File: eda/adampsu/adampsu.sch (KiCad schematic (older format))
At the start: 45 parts, among them J1 Barrel_Jack_Switch, J2 Conn_2Rows-09Pins, J3 DB9_Female, Q1 BUK7880-55A_CUX, SW1 30V 300mA Latching Switch, U1 LM27761, U2 TPS54531DDAR

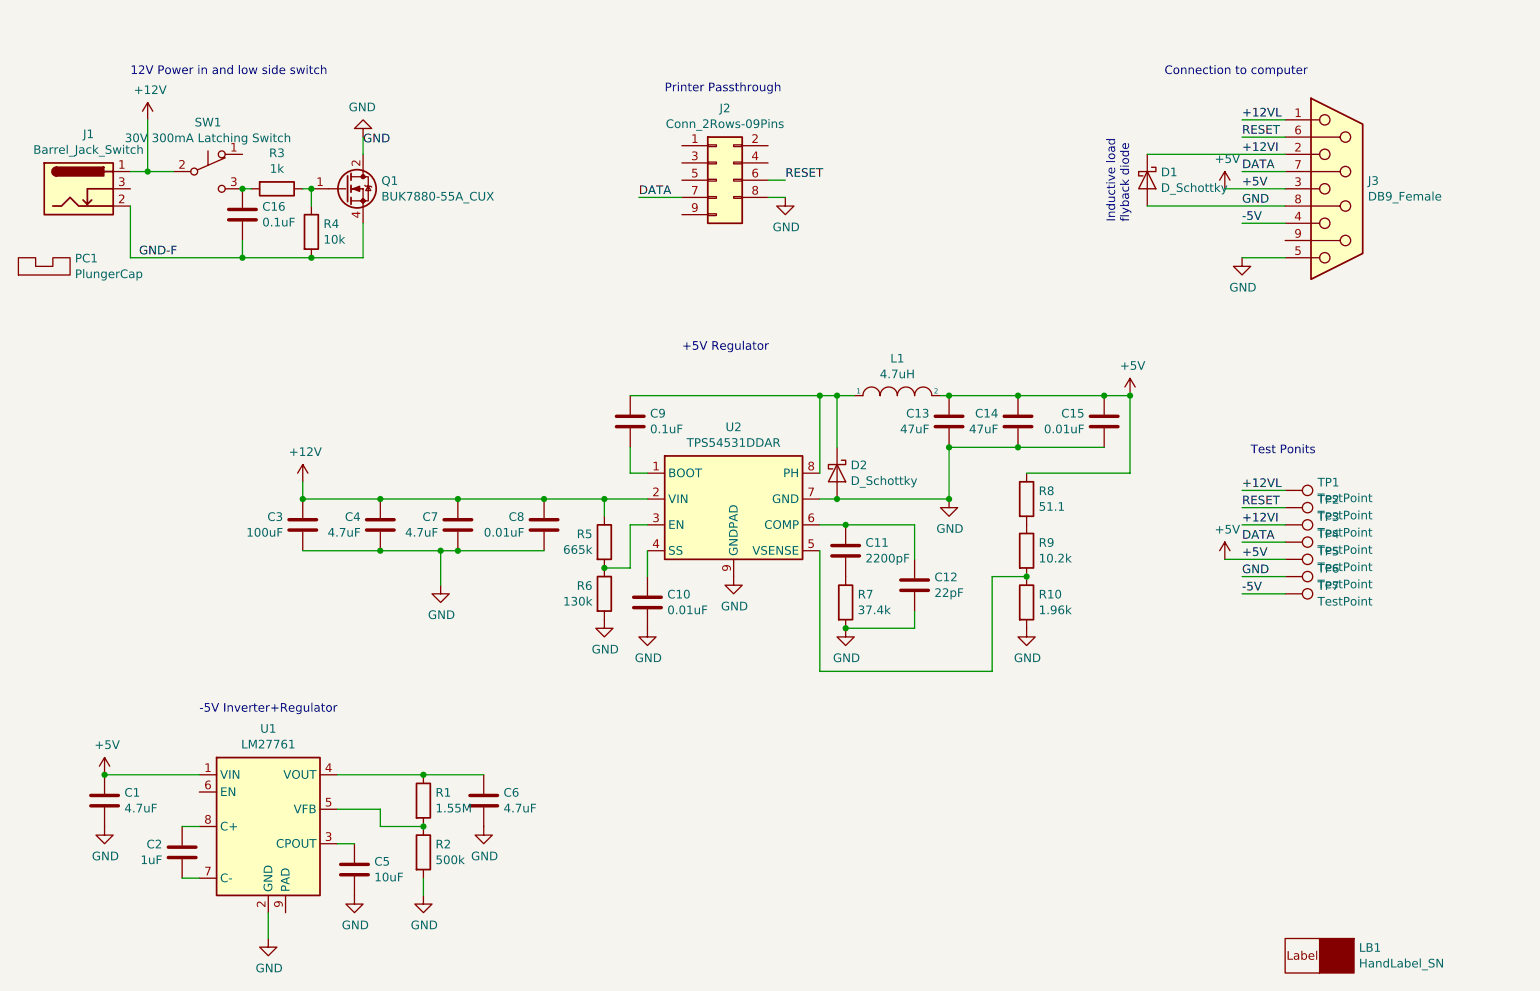
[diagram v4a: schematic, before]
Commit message: using non-inverting buck for negative, too expensive though
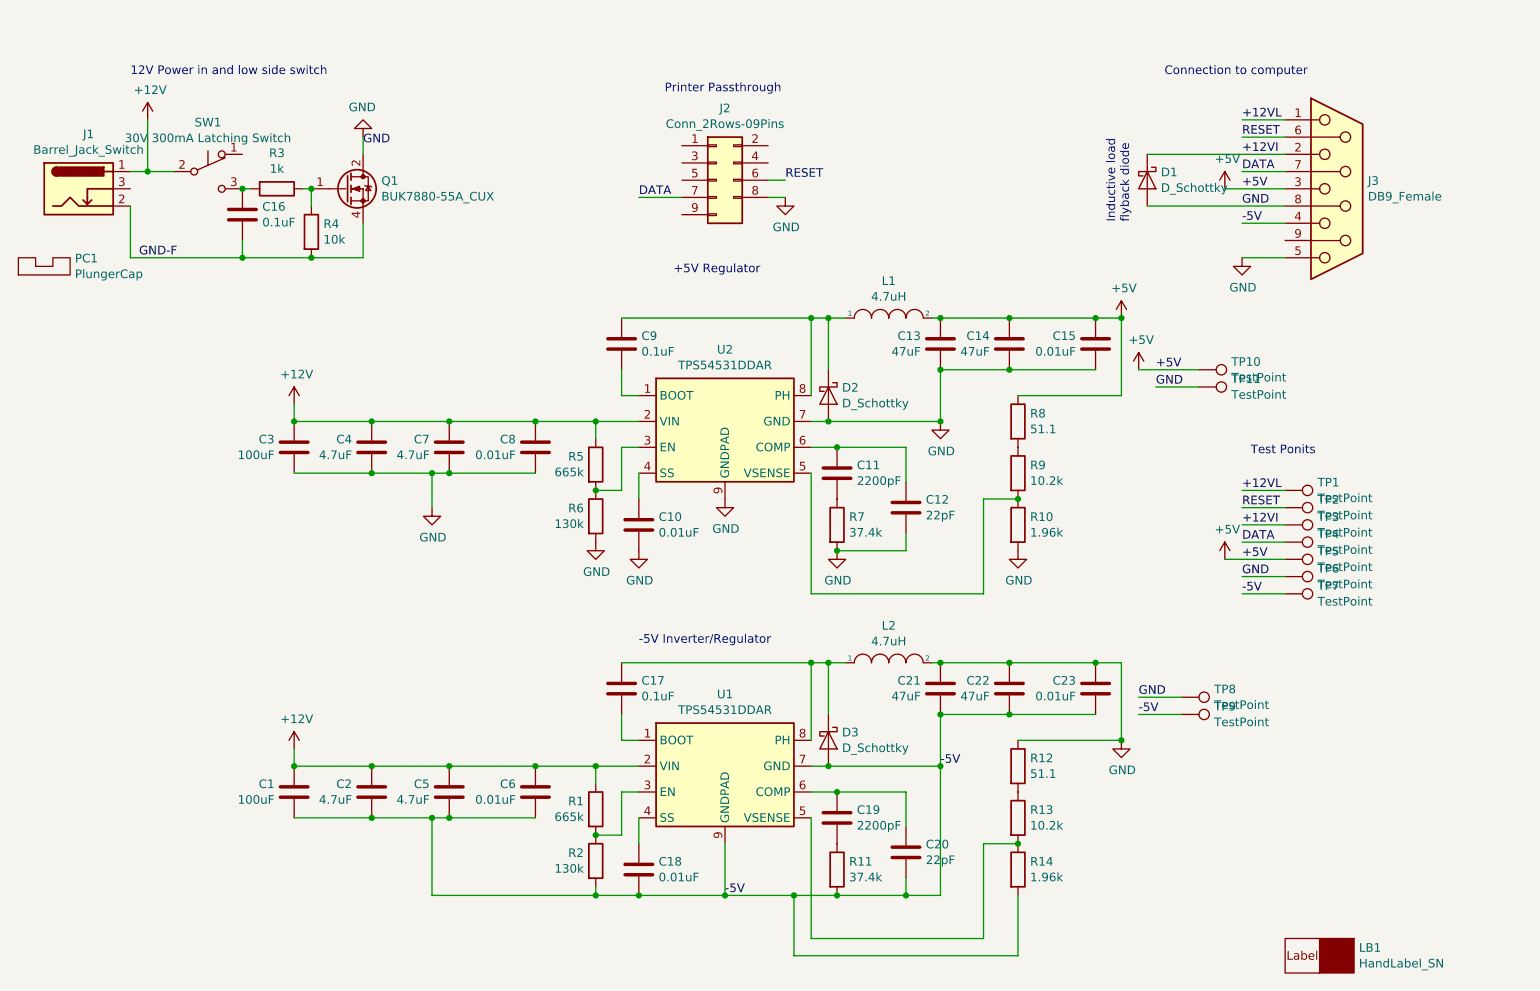
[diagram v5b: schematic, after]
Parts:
- removed R1: 1.55M, Resistor_SMD:R_0603_1608Metric_Pad1.05x0.95mm_HandSolder, symbol adampsu-rescue:R-Device
- removed R2: 500k, Resistor_SMD:R_0603_1608Metric_Pad1.05x0.95mm_HandSolder, symbol adampsu-rescue:R-Device
- removed U1: LM27761, Package_SON:WSON-8-1EP_2x2mm_P0.5mm_EP0.9x1.6mm, symbol adampsu-rescue:LM27761-Regulator_SwitchedCapacitor
- added C17: 0.1uF, adampsu:C_0508_1220Metric_Pad1.40x1.15mm_HandSolder, symbol Device:C
- added C18, C23: 0.01uF, Capacitor_SMD:C_0603_1608Metric_Pad1.05x0.95mm_HandSolder, symbol adampsu-rescue:C-Device
- added C19: 2200pF, Capacitor_SMD:C_0603_1608Metric_Pad1.05x0.95mm_HandSolder, symbol Device:C
- added C20: 22pF, Capacitor_SMD:C_0603_1608Metric_Pad1.05x0.95mm_HandSolder, symbol Device:C
- added C21, C22: 47uF, Capacitor_SMD:C_1210_3225Metric_Pad1.42x2.65mm_HandSolder, symbol adampsu-rescue:C-Device
- added D3: D_Schottky, Diode_SMD:D_SMC_Handsoldering, symbol Device:D_Schottky
- added L2: 4.7uH, adampsu:L_11.5x10.3_H4.8, symbol pspice:INDUCTOR
- added R1: 665k, Resistor_SMD:R_0603_1608Metric_Pad1.05x0.95mm_HandSolder, symbol Device:R
- added R11: 37.4k, Resistor_SMD:R_0603_1608Metric_Pad1.05x0.95mm_HandSolder, symbol Device:R
- added R12: 51.1, Resistor_SMD:R_0603_1608Metric_Pad1.05x0.95mm_HandSolder, symbol Device:R
- added R13: 10.2k, Resistor_SMD:R_0603_1608Metric_Pad1.05x0.95mm_HandSolder, symbol Device:R
- added R14: 1.96k, Resistor_SMD:R_0603_1608Metric_Pad1.05x0.95mm_HandSolder, symbol Device:R
- added R2: 130k, Resistor_SMD:R_0603_1608Metric_Pad1.05x0.95mm_HandSolder, symbol Device:R
- added TP10, TP11, TP8, TP9: TestPoint, TestPoint:TestPoint_THTPad_2.0x2.0mm_Drill1.0mm, symbol Connector:TestPoint
- added U1: TPS54531DDAR, Package_SO:TI_SO-PowerPAD-8_ThermalVias, symbol Custom:TPS54531DDAR
- C1: value 4.7uF -> 100uF; footprint Capacitor_SMD:C_1206_3216Metric_Pad1.42x1.75mm_HandSolder -> Capacitor_Tantalum_SMD:CP_EIA-7343-30_AVX-N_Pad2.25x2.55mm_HandSolder; dk GRM32ER71H475KA88L -> 1189-1659-1-ND; maxV 50 -> 16; mfr UMK316AB7475KL-T -> TAJD107K016TNJV
- C2: value 1uF -> 4.7uF; footprint Capacitor_SMD:C_0603_1608Metric_Pad1.05x0.95mm_HandSolder -> Capacitor_SMD:C_1206_3216Metric_Pad1.42x1.75mm_HandSolder; dk 399-11133-1-ND -> GRM32ER71H475KA88L; maxV 10 -> 50; mfr C0603C105K8RACTU -> UMK316AB7475KL-T
- C3: footprint Capacitor_THT:CP_Radial_D8.0mm_P3.50mm -> Capacitor_Tantalum_SMD:CP_EIA-7343-30_AVX-N_Pad2.25x2.55mm_HandSolder; maxV 50 -> 16; mfr 50YXJ100MT78X11.5 -> TAJD107K016TNJV
- C5: value 10uF -> 4.7uF; footprint Capacitor_SMD:C_0805_2012Metric_Pad1.15x1.40mm_HandSolder -> Capacitor_SMD:C_1206_3216Metric_Pad1.42x1.75mm_HandSolder; dk 490-14381-1-ND -> GRM32ER71H475KA88L; maxV 10+ -> 50; mfr GRM21BR71A106KA73K -> UMK316AB7475KL-T
- C6: value 4.7uF -> 0.01uF; footprint Capacitor_SMD:C_1206_3216Metric_Pad1.42x1.75mm_HandSolder -> Capacitor_SMD:C_0603_1608Metric_Pad1.05x0.95mm_HandSolder; dk GRM32ER71H475KA88L -> 399-7842-1-ND; maxV 50 -> (none); mfr UMK316AB7475KL-T -> C0603C103M5RACTU
- R5: mfr RES SMD 665K OHM 1% 1/10W 0603 -> RC0603FR-07665KL
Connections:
- net +12V: now also C1.1, C2.1, C5.1, C6.1, R1.1, U1.2 (VIN)
- net +5V: now also TP10.1; no longer C1.1
- net -5V: now also C1.2, C2.2, C5.2, C6.2, C18.2, C20.2, C21.2, C22.2, C23.2, D3.2 (A), R11.2, R14.2, R2.2, TP9.1, U1.7 (GND), U1.9 (GNDPAD)
- net GND: now also C21.1, C22.1, C23.1, L2.2, R12.1, TP11.1, TP8.1; no longer C1.2, C5.2, C6.2
- new net: C17.2, U1.1 (BOOT)
- new net: R1.2, R2.1, U1.3 (EN)
- new net: C18.1, U1.4 (SS)
- new net: R13.2, R14.1, U1.5 (VSENSE)
- new net: C19.1, C20.1, U1.6 (COMP)
- new net: C17.1, D3.1 (K), L2.1, U1.8 (PH)
- new net: R12.2, R13.1
- new net: C19.2, R11.1
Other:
- note added: "-5V Inverter/Regulator"
- note removed: "-5V Inverter+Regulator"
- moved on the sheet: C10, C11, C12, C13, C14, C15, C3, C4, C7, C8, C9, D2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

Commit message: Cleanup
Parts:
- removed C1: 100uF, Capacitor_Tantalum_SMD:CP_EIA-7343-30_AVX-N_Pad2.25x2.55mm_HandSolder, symbol adampsu-rescue:C-Device
- removed C13, C14, C21, C22: 47uF, Capacitor_SMD:C_1210_3225Metric_Pad1.42x2.65mm_HandSolder, symbol adampsu-rescue:C-Device
- removed C18, C23, C6: 0.01uF, Capacitor_SMD:C_0603_1608Metric_Pad1.05x0.95mm_HandSolder, symbol adampsu-rescue:C-Device
- removed C2, C5: 4.7uF, Capacitor_SMD:C_1206_3216Metric_Pad1.42x1.75mm_HandSolder, symbol adampsu-rescue:C-Device
- removed D3: D_Schottky, Diode_SMD:D_SMC_Handsoldering, symbol Device:D_Schottky
- removed R12: 51.1, Resistor_SMD:R_0603_1608Metric_Pad1.05x0.95mm_HandSolder, symbol Device:R
- removed R13: 10.2k, Resistor_SMD:R_0603_1608Metric_Pad1.05x0.95mm_HandSolder, symbol Device:R
- removed R14: 1.96k, Resistor_SMD:R_0603_1608Metric_Pad1.05x0.95mm_HandSolder, symbol Device:R
- removed U1: TPS54531DDAR, Package_SO:TI_SO-PowerPAD-8_ThermalVias, symbol Custom:TPS54531DDAR
- added C1, C2: 10uF, Capacitor_SMD:C_0805_2012Metric_Pad1.15x1.40mm_HandSolder, symbol Device:C
- added C13, C14, C18: 22uF, Capacitor_SMD:C_1206_3216Metric_Pad1.42x1.75mm_HandSolder, symbol Device:C
- added C5: 0.1uF, Capacitor_SMD:C_0603_1608Metric_Pad1.05x0.95mm_HandSolder, symbol Device:C
- added C6: 0.1uF, adampsu:C_0508_1220Metric_Pad1.40x1.15mm_HandSolder, symbol Device:C
- added TP12: GND/Green, adampsu:TestPoint_Labeled, symbol Connector:TestPoint
- added U1: TPS561201, Package_TO_SOT_SMD:SOT-23-6_Handsoldering, symbol Custom:TPS561201
- C10, C15, C8: mouser (none) -> 80-C0603C103M5R
- C11: mouser (none) -> 80-C0603C222K5R7411
- C12: mouser (none) -> 581-06035C220JAT2A
- C16: mouser (none) -> 603-CC603KRX7R9BB104
- C17: value 0.1uF -> 22uF; footprint adampsu:C_0508_1220Metric_Pad1.40x1.15mm_HandSolder -> Capacitor_SMD:C_1206_3216Metric_Pad1.42x1.75mm_HandSolder; dk 490-4346-1-ND -> 1276-2728-1-ND; maxV 25 -> (none); mfr LLL216R71E104MA01L -> EMK316ABJ226ML-T; mouser (none) -> 963-EMK316ABJ226ML-T; rating XR7 -> (none)
- C19: value 2200pF -> 22uF; footprint Capacitor_SMD:C_0603_1608Metric_Pad1.05x0.95mm_HandSolder -> Capacitor_SMD:C_1206_3216Metric_Pad1.42x1.75mm_HandSolder; dk 399-17586-1-ND -> 1276-2728-1-ND; maxV 50 -> (none); mfr C0603C222K5RAC7411 -> EMK316ABJ226ML-T; mouser (none) -> 963-EMK316ABJ226ML-T; rating XR7 -> (none)
- C20: value 22pF -> 22uF; footprint Capacitor_SMD:C_0603_1608Metric_Pad1.05x0.95mm_HandSolder -> Capacitor_SMD:C_1206_3216Metric_Pad1.42x1.75mm_HandSolder; dk 478-6204-1-ND -> 1276-2728-1-ND; maxV 50 -> (none); mfr 06035C220JAT2A -> EMK316ABJ226ML-T; mouser (none) -> 963-EMK316ABJ226ML-T; rating XR7 -> (none)
- C3: footprint Capacitor_Tantalum_SMD:CP_EIA-7343-30_AVX-N_Pad2.25x2.55mm_HandSolder -> Capacitor_Tantalum_SMD:CP_EIA-7343-43_Kemet-X_Pad2.25x2.55mm_HandSolder; mouser (none) -> 581-TAJD107K016TNJV
- C4, C7: footprint Capacitor_SMD:C_1206_3216Metric_Pad1.42x1.75mm_HandSolder -> Capacitor_SMD:C_0805_2012Metric_Pad1.15x1.40mm_HandSolder; dk GRM32ER71H475KA88L -> 490-14466-2-ND; mfr UMK316AB7475KL-T -> GRM21BR71C475KE51L; mouser (none) -> 81-GRM21BR71C475KE1L
- C9: mouser (none) -> 81-LLL216R71E104MA1L
- D1, D2: footprint Diode_SMD:D_SMC_Handsoldering -> adampsu:D_SOD-128; dk 641-1126-1-ND -> 1727-5842-1-ND; mfr CDBC540-G -> PMEG4050EP,115; mouser (none) -> 963-EMK325B7226MM-TR
- J1: mouser (none) -> 490-PJ-047AH
- J3: mouser (none) -> 636-171-009-203L001
- L1: mouser (none) -> 673-PA4342.472NLT
- L2: mouser (none) -> 673-PA4342.472NLT; rating 15.5mOhm -> (none)
- PC1: mouser (none) -> 612-4J-WH
- Q1: mouser (none) -> 771-BUK7880-55A/CUX
- R1: value 665k -> 10k; dk 311-665KHRCT-ND -> 311-1.96KHRCT-ND; mfr RC0603FR-07665KL -> RC0603FR-071K96L; mouser (none) -> 603-RC0603FR-071K96L
- R10: mouser (none) -> 603-RC0603FR-071K96L
- R11: value 37.4k -> 54.9k; dk 311-37.4KHRCT-ND -> (none); mfr RC0603FR-0737K4L -> CR0603-FX-5492ELF; mouser (none) -> 652-CR0603FX-5492ELF
- R2: value 130k -> 10k; dk 2019-RK73B1JTTD134JCT-ND -> 311-1.96KHRCT-ND; mfr RK73B1JTTD134J -> RC0603FR-071K96L; mouser (none) -> 603-RC0603FR-071K96L
- R3: mouser (none) -> 603-RC0603JR-071KL
- R4: mouser (none) -> 603-RC0603JR-0710KL
- R5: mouser (none) -> 603-RC0603FR-07665KL
- R6: mouser (none) -> 660-RK73B1JTTD134J
- R7: mouser (none) -> 603-RC0603FR-0737K4L
- R8: mouser (none) -> 603-RC0603FR-0751R1L
- R9: mouser (none) -> 667-ERJ-3EKF1022V
- SW1: mouser (none) -> 612-LC1258EENP
- TP1: value TestPoint -> +12VL/Orange; footprint TestPoint:TestPoint_THTPad_2.0x2.0mm_Drill1.0mm -> adampsu:TestPoint_Labeled
- TP10: value TestPoint -> +5V; footprint TestPoint:TestPoint_THTPad_2.0x2.0mm_Drill1.0mm -> adampsu:TestPoint_Labeled
- TP11, TP8: value TestPoint -> GND; footprint TestPoint:TestPoint_THTPad_2.0x2.0mm_Drill1.0mm -> adampsu:TestPoint_Labeled
- TP2: value TestPoint -> RESET/Black; footprint TestPoint:TestPoint_THTPad_2.0x2.0mm_Drill1.0mm -> adampsu:TestPoint_Labeled
- TP3: value TestPoint -> +12VI/Yellow; footprint TestPoint:TestPoint_THTPad_2.0x2.0mm_Drill1.0mm -> adampsu:TestPoint_Labeled
- TP4: value TestPoint -> DATA/Brown; footprint TestPoint:TestPoint_THTPad_2.0x2.0mm_Drill1.0mm -> adampsu:TestPoint_Labeled
- TP5: value TestPoint -> +5V/Red; footprint TestPoint:TestPoint_THTPad_2.0x2.0mm_Drill1.0mm -> adampsu:TestPoint_Labeled
- TP6: value TestPoint -> GND/Green; footprint TestPoint:TestPoint_THTPad_2.0x2.0mm_Drill1.0mm -> adampsu:TestPoint_Labeled
- TP7: value TestPoint -> -5V/Blue; footprint TestPoint:TestPoint_THTPad_2.0x2.0mm_Drill1.0mm -> adampsu:TestPoint_Labeled
- TP9: value TestPoint -> -5V; footprint TestPoint:TestPoint_THTPad_2.0x2.0mm_Drill1.0mm -> adampsu:TestPoint_Labeled
- U2: mouser (none) -> 595-TPS54531DDAR
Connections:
- net +12VI is gone; now on net +12V: D1.1 (K), J3.2, TP3.1
- net +12VL is gone; now on net +12V: J3.1, TP1.1
- net +12V: now also C1.1, C2.1, C5.1, U1.3 (VIN); no longer R1.1
- net +5V: now also C19.1, C20.2, C13.1, C14.2
- net -5V: now also C17.2, R2.1, C18.2, U1.1 (GND); no longer C20.2, R11.2, R2.2
- net GND: now also C17.1, C19.2, C20.1, R1.1, R11.1, C1.2, C13.2, C14.1, C18.1, C2.2, C5.2, TP12.1
- net PH: now reaches C9.1, D2.1 (K), L1.1, U2.8 (PH)
- net at R1.2: now also U1.5 (EN); no longer R2.1
- net SW: now reaches L2.1
- net SW: now also C6.2, U1.2 (SW); no longer C17.1
- new net: R11.2, R2.2, U1.4 (VFB)
- new net: C6.1, U1.6 (VBST)
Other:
- note added: "Test Points"
- note removed: "Test Ponits"
- moved on the sheet: R10, R8, R9, TP1, TP10, TP11, TP3, TP4, TP5, TP6, TP7, TP8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

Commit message: Export schematic and PCB to PDFs
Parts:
- R4: value 10k -> 1k; dk 311-10KGRCT-ND -> 311-1.0KGRCT-ND; mfr RC0603JR-0710KL -> RC0603JR-071KL; mouser 603-RC0603JR-0710KL -> 603-RC0603JR-071KL
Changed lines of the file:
@@
 Wire Wire Line
 	2250 1500 2300 1500
-$Comp
-L Device:R R4
-U 1 1 5DBAB23A
-P 2300 1750
-F 0 "R4" H 2370 1796 50  0000 L CNN
-F 1 "10k" H 2370 1705 50  0000 L CNN
-F 2 "Resistor_SMD:R_0603_1608Metric_Pad1.05x0.95mm_HandSolder" V 2230 1750 50  0001 C CNN
-F 3 "http://www.yageo.com/documents/recent/PYu-RC_Group_51_RoHS_L_10.pdf" H 2300 1750 50  0001 C CNN
-F 4 "311-10KGRCT-ND" H 2300 1750 50  0001 C CNN "dk"
-F 5 "RC0603JR-0710KL" H 2300 1750 50  0001 C CNN "mfr"
-F 6 "603-RC0603JR-0710KL" H 2300 1750 50  0001 C CNN "mouser"
-	1    2300 1750
-	1    0    0    -1
-$EndComp
 Wire Wire Line
 	2300 1500 2300 1600
@@
 	2600 1700 2600 1900
 Wire Wire Line
-	2600 1900 2300 1900
-Wire Wire Line
-	2300 1900 1900 1900
-Wire Wire Line
 	1250 1900 1250 1600
-Connection ~ 2300 1900
 Text Label 1300 1900 0    50   ~ 0
 GND-F
@@
 	0    1    1    0
 $EndComp
+$Comp
+L Device:R R4
+U 1 1 5DCAA07F
+P 2300 1750
+F 0 "R4" H 2370 1796 50  0000 L CNN
+F 1 "1k" H 2370 1705 50  0000 L CNN
+F 2 "Resistor_SMD:R_0603_1608Metric_Pad1.05x0.95mm_HandSolder" V 2230 1750 50  0001 C CNN
+F 3 "http://www.yageo.com/documents/recent/PYu-RC_Group_51_RoHS_L_10.pdf" H 2300 1750 50  0001 C CNN
+F 4 "311-1.0KGRCT-ND" H 2300 1750 50  0001 C CNN "dk"
+F 5 "RC0603JR-071KL" H 2300 1750 50  0001 C CNN "mfr"
+F 6 "603-RC0603JR-071KL" H 2300 1750 50  0001 C CNN "mouser"
+	1    2300 1750
+	1    0    0    -1
+$EndComp
+Wire Wire Line
+	1900 1900 2300 1900
+Connection ~ 2300 1900
+Wire Wire Line
+	2300 1900 2600 1900
 $EndSCHEMATC

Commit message: high side switching
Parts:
- removed Q1: BUK7880-55A_CUX, Package_TO_SOT_SMD:SOT-223-3_TabPin2, symbol Custom:BUK7880-55A_CUX
- added C21, C22: 22uF, Capacitor_SMD:C_1206_3216Metric_Pad1.42x1.75mm_HandSolder, symbol Device:C
- added Q1: Si4447ADY, Package_SO:SO-8_3.9x4.9mm_P1.27mm, symbol Custom:Si4447ADY
- added Q2: Q_NPN_BEC, Package_TO_SOT_SMD:SOT-23, symbol Device:Q_NPN_BEC
- added R12: 100k, Resistor_SMD:R_0603_1608Metric_Pad1.05x0.95mm_HandSolder, symbol Device:R
- added U3: Cuts, adampsu:DB9-SpotMount, symbol Custom:Cuts
- R4: value 1k -> 100k; dk 311-1.0KGRCT-ND -> (none); mfr RC0603JR-071KL -> (none); mouser 603-RC0603JR-071KL -> (none)
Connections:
- net +12V: now also R1.1, Q1.5 (D), Q1.6 (D), Q1.7 (D), Q1.8 (D); no longer J1.1, SW1.2 (B)
- net -5V: now also C21.2, C22.2
- net GND: now also C16.2, J1.2, SW1.3 (C), C21.1, C22.1, Q2.2 (E); no longer R1.1
- net at SW1.1 (A): now also R12.2
- net at C16.1, R3.2: now also Q2.1 (B); no longer SW1.3 (C)
- net at R3.1: now also SW1.2 (B); no longer R4.1
- removed net GND-F: C16.2, J1.2, R4.2
- new net: Q1.4 (G), Q2.3 (C), R4.2
- new net 12V-IN: J1.1, Q1.1 (S), Q1.2 (S), Q1.3 (S), R12.1, R4.1
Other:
- note added: "12V Power in and high side switch"
- note removed: "12V Power in and low side switch"
- moved on the sheet: C16, R1, R3, SW1
